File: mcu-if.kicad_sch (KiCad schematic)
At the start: 46 parts, among them J501 MCU_USB, J502 SD_Card, J503 CONN_DISP, J504 RJ45_Amphenol_RJMG1BD3B8K1ANR, SW501 BTN0, SW502 BTN1, SW503 BTN2, SW504 BTN3, U501 KSZ8081RNA

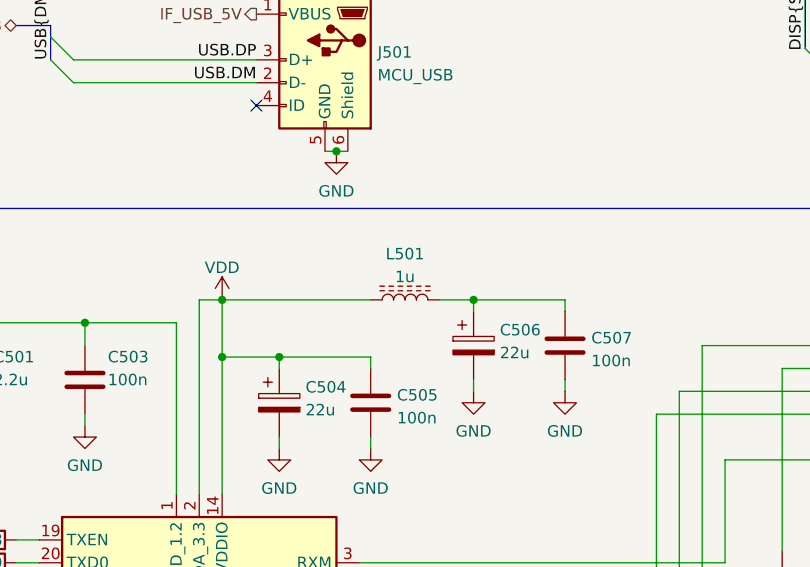
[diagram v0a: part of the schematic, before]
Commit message: Re-annotation, footprints
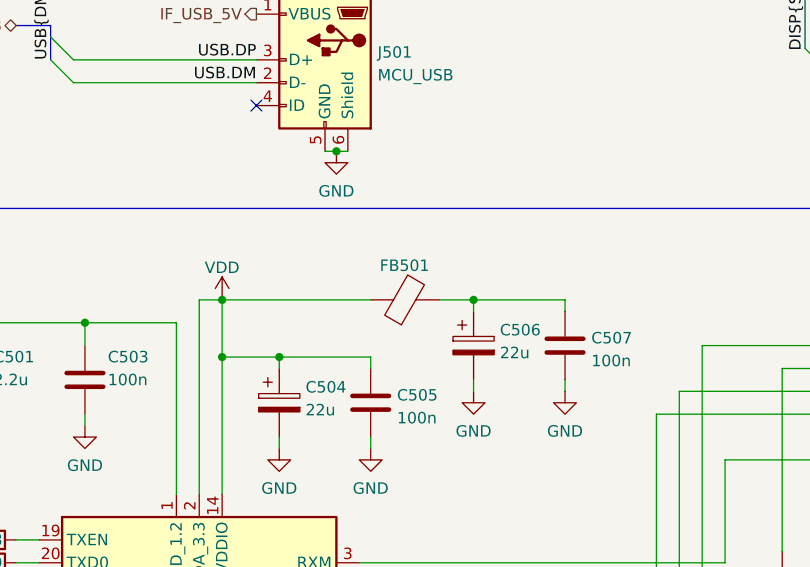
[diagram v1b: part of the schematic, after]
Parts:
- removed L501: 1u, symbol Device:L_Ferrite
- added FB501: FerriteBead, Inductor_SMD:L_0603_1608Metric_Pad1.05x0.95mm_HandSolder, symbol Device:FerriteBead
- J501: footprint (none) -> Connector_USB:USB_Mini-B_Wuerth_65100516121_Horizontal
- R501, R502, R503, R504, R505, R506, R507, R508, R509, R510, R511, R512, R513, R514, R515, R516, R517, R518, R519, R520, R521, R522, R523, R524, R525: footprint (none) -> Resistor_SMD:R_0603_1608Metric_Pad0.98x0.95mm_HandSolder
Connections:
- net VDD: now also FB501.1
- net at C506.1, C507.1: now also FB501.2
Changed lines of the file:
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@@
     (property "Reference" "R508" (id 0) (at 64.77 137.16 90))
     (property "Value" "0" (id 1) (at 59.69 135.89 90))
-    (property "Footprint" "" (id 2) (at 64.77 138.938 90)
+    (property "Footprint" "Resistor_SMD:R_0603_1608Metric_Pad0.98x0.95mm_HandSolder" (id 2) (at 64.77 138.938 90)
       (effects (font (size 1.27 1.27)) hide)
     )
@@
       (effects (font (size 1.27 1.27)) (justify left))
     )
-    (property "Footprint" "" (id 2) (at 245.872 43.18 90)
+    (property "Footprint" "Resistor_SMD:R_0603_1608Metric_Pad0.98x0.95mm_HandSolder" (id 2) (at 245.872 43.18 90)
       (effects (font (size 1.27 1.27)) hide)
     )
@@
     (property "Reference" "R514" (id 0) (at 64.77 154.94 90))
     (property "Value" "0" (id 1) (at 59.69 153.67 90))
-    (property "Footprint" "" (id 2) (at 64.77 156.718 90)
+    (property "Footprint" "Resistor_SMD:R_0603_1608Metric_Pad0.98x0.95mm_HandSolder" (id 2) (at 64.77 156.718 90)
       (effects (font (size 1.27 1.27)) hide)
     )
@@
     )
     (pin "1")
-  )
-  (symbol (lib_id "Device:L_Ferrite") (at 111.76 110.49 90) (unit 1)
-    (in_bom yes) (on_board yes) (fields_autoplaced)
-    (property "Reference" "L501" (id 0) (at 111.76 105.3932 90))
-    (property "Value" "1u" (id 1) (at 111.76 107.9301 90))
-    (property "Footprint" "" (id 2) (at 111.76 110.49 0)
-      (effects (font (size 1.27 1.27)) hide)
-    )
-    (property "Datasheet" "~" (id 3) (at 111.76 110.49 0)
-      (effects (font (size 1.27 1.27)) hide)
-    )
-    (pin "1")
-    (pin "2")
   )
   (symbol (lib_id "Switch:SW_Push") (at 203.2 27.94 90) (unit 1)
@@
       (effects (font (size 1.27 1.27)) (justify right))
     )
-    (property "Footprint" "" (id 2) (at 187.198 43.18 90)
+    (property "Footprint" "Resistor_SMD:R_0603_1608Metric_Pad0.98x0.95mm_HandSolder" (id 2) (at 187.198 43.18 90)
       (effects (font (size 1.27 1.27)) hide)
     )
@@
     (pin "1")
   )
+  (symbol (lib_id "Device:FerriteBead") (at 111.76 110.49 90) (unit 1)
+    (in_bom yes) (on_board yes) (fields_autoplaced)
+    (property "Reference" "FB501" (id 0) (at 111.7092 106.6856 90))
+    (property "Value" "FerriteBead" (id 1) (at 111.7092 106.6855 90)
+      (effects (font (size 1.27 1.27)) hide)
+    )
+    (property "Footprint" "Inductor_SMD:L_0603_1608Metric_Pad1.05x0.95mm_HandSolder" (id 2) (at 111.76 112.268 90)
+      (effects (font (size 1.27 1.27)) hide)
+    )
+    (property "Datasheet" "~" (id 3) (at 111.76 110.49 0)
+      (effects (font (size 1.27 1.27)) hide)
+    )
+    (property "Part" "815-ACML-0603H-301" (id 4) (at 111.76 110.49 90)
+      (effects (font (size 1.27 1.27)) hide)
+    )
+    (pin "1")
+    (pin "2")
+  )
   (symbol (lib_id "power:GND") (at 88.9 187.96 0) (unit 1)
     (in_bom yes) (on_board yes) (fields_autoplaced)
@@
     (property "Reference" "R515" (id 0) (at 86.36 55.88 90))
     (property "Value" "100" (id 1) (at 86.36 53.7011 90))
-    (property "Footprint" "" (id 2) (at 86.36 57.658 90)
+    (property "Footprint" "Resistor_SMD:R_0603_1608Metric_Pad0.98x0.95mm_HandSolder" (id 2) (at 86.36 57.658 90)
       (effects (font (size 1.27 1.27)) hide)
     )
@@
     (property "Reference" "R504" (id 0) (at 54.61 157.48 90))
     (property "Value" "10k" (id 1) (at 54.61 160.02 90))
-    (property "Footprint" "" (id 2) (at 54.61 159.258 90)
+    (property "Footprint" "Resistor_SMD:R_0603_1608Metric_Pad0.98x0.95mm_HandSolder" (id 2) (at 54.61 159.258 90)
       (effects (font (size 1.27 1.27)) hide)
     )
@@
     (property "Reference" "R510" (id 0) (at 64.77 142.24 90))
     (property "Value" "0" (id 1) (at 59.69 140.97 90))
-    (property "Footprint" "" (id 2) (at 64.77 144.018 90)
+    (property "Footprint" "Resistor_SMD:R_0603_1608Metric_Pad0.98x0.95mm_HandSolder" (id 2) (at 64.77 144.018 90)
       (effects (font (size 1.27 1.27)) hide)
     )
@@
     (property "Reference" "R512" (id 0) (at 64.77 149.86 90))
     (property "Value" "0" (id 1) (at 59.69 148.59 90))
-    (property "Footprint" "" (id 2) (at 64.77 151.638 90)
+    (property "Footprint" "Resistor_SMD:R_0603_1608Metric_Pad0.98x0.95mm_HandSolder" (id 2) (at 64.77 151.638 90)
       (effects (font (size 1.27 1.27)) hide)
     )
@@
     (property "Reference" "R516" (id 0) (at 114.3 170.18 90))
     (property "Value" "6.49k" (id 1) (at 114.3 168.0011 90))
-    (property "Footprint" "" (id 2) (at 114.3 171.958 90)
+    (property "Footprint" "Resistor_SMD:R_0603_1608Metric_Pad0.98x0.95mm_HandSolder" (id 2) (at 114.3 171.958 90)
       (effects (font (size 1.27 1.27)) hide)
     )
@@
       (effects (font (size 1.27 1.27)) (justify left))
     )
-    (property "Footprint" "" (id 2) (at 56.642 38.1 90)
+    (property "Footprint" "Resistor_SMD:R_0603_1608Metric_Pad0.98x0.95mm_HandSolder" (id 2) (at 56.642 38.1 90)
       (effects (font (size 1.27 1.27)) hide)
     )
@@
       (effects (font (size 1.27 1.27)) (justify left))
     )
-    (property "Footprint" "" (id 2) (at 31.242 30.48 90)
+    (property "Footprint" "Resistor_SMD:R_0603_1608Metric_Pad0.98x0.95mm_HandSolder" (id 2) (at 31.242 30.48 90)
       (effects (font (size 1.27 1.27)) hide)
     )
@@
       (effects (font (size 1.27 1.27)) (justify left))
     )
-    (property "Footprint" "" (id 2) (at 186.182 146.05 90)
+    (property "Footprint" "Resistor_SMD:R_0603_1608Metric_Pad0.98x0.95mm_HandSolder" (id 2) (at 186.182 146.05 90)
       (effects (font (size 1.27 1.27)) hide)
     )
@@
     (property "Reference" "R505" (id 0) (at 54.61 180.34 90))
     (property "Value" "100" (id 1) (at 54.61 178.1611 90))
-    (property "Footprint" "" (id 2) (at 54.61 182.118 90)
+    (property "Footprint" "Resistor_SMD:R_0603_1608Metric_Pad0.98x0.95mm_HandSolder" (id 2) (at 54.61 182.118 90)
       (effects (font (size 1.27 1.27)) hide)
     )
@@
       (effects (font (size 1.27 1.27)) (justify right))
     )
-    (property "Footprint" "" (id 2) (at 99.06 85.09 0)
+    (property "Footprint" "Connector_USB:USB_Mini-B_Wuerth_65100516121_Horizontal" (id 2) (at 99.06 85.09 0)
       (effects (font (size 1.27 1.27)) hide)
     )
@@
       (effects (font (size 1.27 1.27)) (justify left))
     )
-    (property "Footprint" "" (id 2) (at 174.752 158.75 90)
+    (property "Footprint" "Resistor_SMD:R_0603_1608Metric_Pad0.98x0.95mm_HandSolder" (id 2) (at 174.752 158.75 90)
       (effects (font (size 1.27 1.27)) hide)
     )
@@
       (effects (font (size 1.27 1.27)) (justify left))
     )
-    (property "Footprint" "" (id 2) (at 174.752 146.05 90)
+    (property "Footprint" "Resistor_SMD:R_0603_1608Metric_Pad0.98x0.95mm_HandSolder" (id 2) (at 174.752 146.05 90)
       (effects (font (size 1.27 1.27)) hide)
     )
@@
       (effects (font (size 1.27 1.27)) (justify right))
     )
-    (property "Footprint" "" (id 2) (at 177.038 43.18 90)
+    (property "Footprint" "Resistor_SMD:R_0603_1608Metric_Pad0.98x0.95mm_HandSolder" (id 2) (at 177.038 43.18 90)
       (effects (font (size 1.27 1.27)) hide)
     )
@@
       (effects (font (size 1.27 1.27)) (justify right))
     )
-    (property "Footprint" "" (id 2) (at 204.978 43.18 90)
+    (property "Footprint" "Resistor_SMD:R_0603_1608Metric_Pad0.98x0.95mm_HandSolder" (id 2) (at 204.978 43.18 90)
       (effects (font (size 1.27 1.27)) hide)
     )
@@
       (effects (font (size 1.27 1.27)) (justify left))
     )
-    (property "Footprint" "" (id 2) (at 43.942 30.48 90)
+    (property "Footprint" "Resistor_SMD:R_0603_1608Metric_Pad0.98x0.95mm_HandSolder" (id 2) (at 43.942 30.48 90)
       (effects (font (size 1.27 1.27)) hide)
     )
@@
     (property "Reference" "R511" (id 0) (at 64.77 147.32 90))
     (property "Value" "0" (id 1) (at 59.69 146.05 90))
-    (property "Footprint" "" (id 2) (at 64.77 149.098 90)
+    (property "Footprint" "Resistor_SMD:R_0603_1608Metric_Pad0.98x0.95mm_HandSolder" (id 2) (at 64.77 149.098 90)
       (effects (font (size 1.27 1.27)) hide)
     )
@@
       (effects (font (size 1.27 1.27)) (justify left))
     )
-    (property "Footprint" "" (id 2) (at 236.982 43.18 90)
+    (property "Footprint" "Resistor_SMD:R_0603_1608Metric_Pad0.98x0.95mm_HandSolder" (id 2) (at 236.982 43.18 90)
       (effects (font (size 1.27 1.27)) hide)
     )
@@
       (effects (font (size 1.27 1.27)) (justify left))
     )
-    (property "Footprint" "" (id 2) (at 62.992 30.48 90)
+    (property "Footprint" "Resistor_SMD:R_0603_1608Metric_Pad0.98x0.95mm_HandSolder" (id 2) (at 62.992 30.48 90)
       (effects (font (size 1.27 1.27)) hide)
     )
@@
     (property "Reference" "R513" (id 0) (at 64.77 152.4 90))
     (property "Value" "0" (id 1) (at 59.69 151.13 90))
-    (property "Footprint" "" (id 2) (at 64.77 154.178 90)
+    (property "Footprint" "Resistor_SMD:R_0603_1608Metric_Pad0.98x0.95mm_HandSolder" (id 2) (at 64.77 154.178 90)
       (effects (font (size 1.27 1.27)) hide)
     )
@@
       (effects (font (size 1.27 1.27)) (justify right))
     )
-    (property "Footprint" "" (id 2) (at 196.088 43.18 90)
+    (property "Footprint" "Resistor_SMD:R_0603_1608Metric_Pad0.98x0.95mm_HandSolder" (id 2) (at 196.088 43.18 90)
       (effects (font (size 1.27 1.27)) hide)
     )
@@
     (property "Reference" "R509" (id 0) (at 64.77 139.7 90))
     (property "Value" "0" (id 1) (at 59.69 138.43 90))
-    (property "Footprint" "" (id 2) (at 64.77 141.478 90)
+    (property "Footprint" "Resistor_SMD:R_0603_1608Metric_Pad0.98x0.95mm_HandSolder" (id 2) (at 64.77 141.478 90)
       (effects (font (size 1.27 1.27)) hide)
     )
@@
       (effects (font (size 1.27 1.27)) (justify left))
     )
-    (property "Footprint" "" (id 2) (at 37.592 38.1 90)
-      (effects (font (size 1.27 1.27)) hide)
-    )
+    (property "Footprint" "Resistor_SMD:R_0603_1608Metric_Pad0.98x0.95mm_HandSolder" (id 2) (at 37.592 38.1 90)
+      (effects (font (size 1.27 1.27)) hide)
+    )

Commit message: Add button footprint
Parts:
- SW501, SW502, SW503, SW504: footprint (none) -> marco-ram-board:DTSMW69N
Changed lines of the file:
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@@
       (effects (font (size 1.27 1.27)) (justify right))
     )
-    (property "Footprint" "" (id 2) (at 189.23 27.94 0)
+    (property "Footprint" "marco-ram-board:DTSMW69N" (id 2) (at 189.23 27.94 0)
       (effects (font (size 1.27 1.27)) hide)
     )
@@
       (effects (font (size 1.27 1.27)) (justify right))
     )
-    (property "Footprint" "" (id 2) (at 198.12 27.94 0)
+    (property "Footprint" "marco-ram-board:DTSMW69N" (id 2) (at 198.12 27.94 0)
       (effects (font (size 1.27 1.27)) hide)
     )
@@
       (effects (font (size 1.27 1.27)) (justify right))
     )
-    (property "Footprint" "" (id 2) (at 180.34 27.94 0)
+    (property "Footprint" "marco-ram-board:DTSMW69N" (id 2) (at 180.34 27.94 0)
       (effects (font (size 1.27 1.27)) hide)
     )
@@
       (effects (font (size 1.27 1.27)) (justify right))
     )
-    (property "Footprint" "" (id 2) (at 170.18 27.94 0)
-      (effects (font (size 1.27 1.27)) hide)
-    )
+    (property "Footprint" "marco-ram-board:DTSMW69N" (id 2) (at 170.18 27.94 0)
+      (effects (font (size 1.27 1.27)) hide)
+    )

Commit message: More footprints
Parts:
- J502: footprint (none) -> Connector_Card:SD_Hirose_DM1AA_SF_PEJ82
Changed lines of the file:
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@@
+    (stroke (width 0) (type default) (color 0 0 0 0))
+  )
+  (wire (pts (xy 91.44 109.22) (xy 91.44 110.49))
     (stroke (width 0) (type default) (color 0 0 0 0))
   )
@@
     (pin "2")
   )
-  (symbol (lib_id "power:VDD") (at 91.44 110.49 0) (unit 1)
-    (in_bom yes) (on_board yes) (fields_autoplaced)
-    (property "Reference" "#PWR0507" (id 0) (at 91.44 114.3 0)
-      (effects (font (size 1.27 1.27)) hide)
-    )
-    (property "Value" "VDD" (id 1) (at 91.44 106.9142 0))
-    (property "Footprint" "" (id 2) (at 91.44 110.49 0)
-      (effects (font (size 1.27 1.27)) hide)
-    )
-    (property "Datasheet" "" (id 3) (at 91.44 110.49 0)
+  (symbol (lib_id "power:VDD") (at 91.44 109.22 0) (unit 1)
+    (in_bom yes) (on_board yes) (fields_autoplaced)
+    (property "Reference" "#PWR0507" (id 0) (at 91.44 113.03 0)
+      (effects (font (size 1.27 1.27)) hide)
+    )
+    (property "Value" "VDD" (id 1) (at 91.44 105.6442 0))
+    (property "Footprint" "" (id 2) (at 91.44 109.22 0)
+      (effects (font (size 1.27 1.27)) hide)
+    )
+    (property "Datasheet" "" (id 3) (at 91.44 109.22 0)
       (effects (font (size 1.27 1.27)) hide)
     )
@@
   )
   (symbol (lib_id "Device:C_Polarized") (at 119.38 115.57 0) (unit 1)
-    (in_bom yes) (on_board yes) (fields_autoplaced)
-    (property "Reference" "C506" (id 0) (at 122.301 113.8463 0)
-      (effects (font (size 1.27 1.27)) (justify left))
-    )
-    (property "Value" "22u" (id 1) (at 122.301 116.3832 0)
+    (in_bom yes) (on_board yes)
+    (property "Reference" "C506" (id 0) (at 121.92 113.03 0)
+      (effects (font (size 1.27 1.27)) (justify left))
+    )
+    (property "Value" "22u" (id 1) (at 121.92 115.5669 0)
       (effects (font (size 1.27 1.27)) (justify left))
     )
@@
     (property "Reference" "J502" (id 0) (at 113.03 37.0672 0))
     (property "Value" "SD_Card" (id 1) (at 113.03 39.6041 0))
-    (property "Footprint" "" (id 2) (at 113.03 53.34 0)
+    (property "Footprint" "Connector_Card:SD_Hirose_DM1AA_SF_PEJ82" (id 2) (at 113.03 53.34 0)
       (effects (font (size 1.27 1.27)) hide)
     )
@@
   )
   (symbol (lib_id "Device:C_Polarized") (at 97.79 121.92 0) (unit 1)
-    (in_bom yes) (on_board yes) (fields_autoplaced)
-    (property "Reference" "C504" (id 0) (at 100.711 120.1963 0)
-      (effects (font (size 1.27 1.27)) (justify left))
-    )
-    (property "Value" "22u" (id 1) (at 100.711 122.7332 0)
+    (in_bom yes) (on_board yes)
+    (property "Reference" "C504" (id 0) (at 100.33 119.3831 0)
+      (effects (font (size 1.27 1.27)) (justify left))
+    )
+    (property "Value" "22u" (id 1) (at 100.33 121.92 0)
       (effects (font (size 1.27 1.27)) (justify left))
     )
@@
   )
   (symbol (lib_id "Device:C") (at 107.95 121.92 0) (unit 1)
-    (in_bom yes) (on_board yes) (fields_autoplaced)
-    (property "Reference" "C505" (id 0) (at 110.871 121.0853 0)
-      (effects (font (size 1.27 1.27)) (justify left))
-    )
-    (property "Value" "100n" (id 1) (at 110.871 123.6222 0)
+    (in_bom yes) (on_board yes)
+    (property "Reference" "C505" (id 0) (at 110.49 119.3831 0)
+      (effects (font (size 1.27 1.27)) (justify left))
+    )
+    (property "Value" "100n" (id 1) (at 110.49 121.92 0)
       (effects (font (size 1.27 1.27)) (justify left))
     )
@@
   (symbol (lib_id "Device:C") (at 129.54 115.57 0) (unit 1)
     (in_bom yes) (on_board yes)
-    (property "Reference" "C507" (id 0) (at 132.461 114.7353 0)
-      (effects (font (size 1.27 1.27)) (justify left))
-    )
-    (property "Value" "100n" (id 1) (at 132.461 117.2722 0)
-      (effects (font (size 1.27 1.27)) (justify left))
-    )
+    (property "Reference" "C507" (id 0) (at 132.08 113.03 0)
+      (effects (font (size 1.27 1.27)) (justify left))
+    )
+    (property "Value" "100n" (id 1) (at 132.08 115.5669 0)
+      (effects (font (size 1.27 1.27)) (justify left))
+    )
